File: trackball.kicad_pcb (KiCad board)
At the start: 2 copper layers, 27.5 x 35.2 mm, 38 parts, among them P1 CONN_10, P2 CONN_5, U1 MKL03Z32VFK4, U2 ADNS-3530, U4 ESD

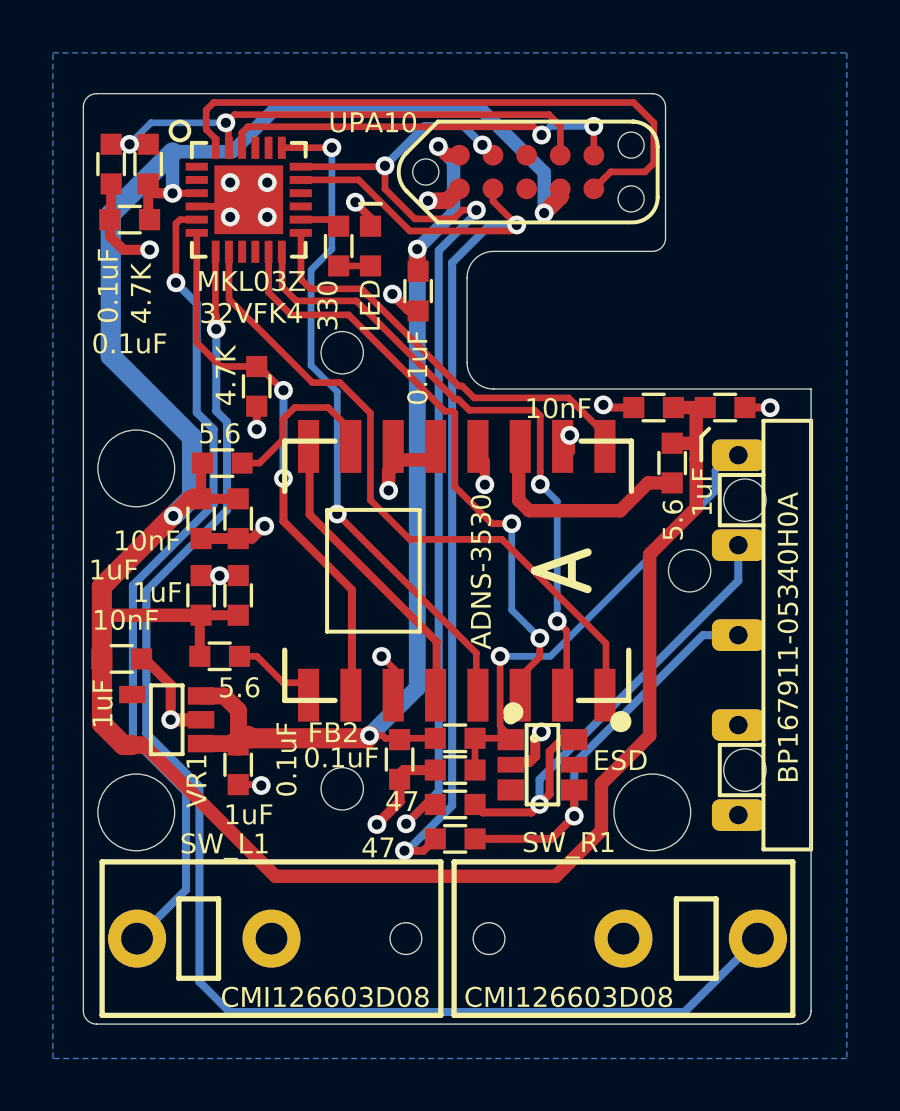
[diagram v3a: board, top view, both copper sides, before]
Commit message: Add additional silk screen content for the sensor.
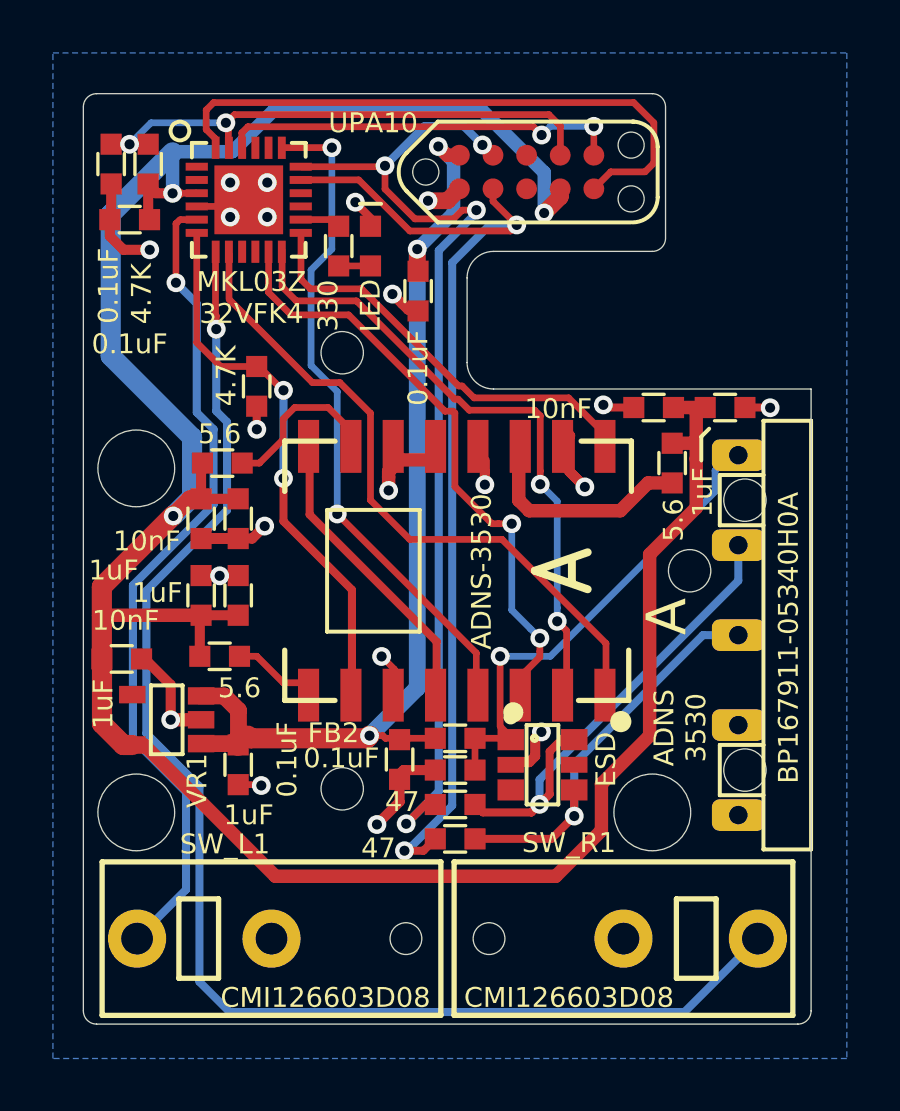
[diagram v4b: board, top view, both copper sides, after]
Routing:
- net GND: track 34.3 -> 37.0 mm
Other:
- board text added: "A"
- board text added: "ADNS 3530"
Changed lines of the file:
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@@
   (general
     (thickness 1.6)
-    (drawings 45)
-    (tracks 399)
+    (drawings 47)
+    (tracks 402)
     (zones 0)
     (modules 38)
@@
       (effects (font (size 0.75 0.75) (thickness 0.15)))
     )
-    (fp_text value ESD (at -0.15 -2.95 180) (layer F.SilkS)
+    (fp_text value ESD (at -0.2 -2.4 270) (layer F.SilkS)
       (effects (font (size 0.75 0.75) (thickness 0.15)))
     )
@@
     (pad 1 thru_hole roundrect (at -2.75 -6.8) (size 2 1.2) (drill 0.7) (layers *.Cu *.Mask) (roundrect_rratio 0.25)
       (net 4 /VCC_BOTTOM) (clearance 0.0762))
+  )
+  (gr_text "ADNS\n3530" (at 204.7 136.5 90) (layer F.SilkS)
+    (effects (font (size 0.75 0.75) (thickness 0.15)))
+  )
+  (gr_text A (at 204.2 132.3 90) (layer F.SilkS)
+    (effects (font (size 1.5 1.5) (thickness 0.3)) (justify mirror))
   )
   (gr_circle (center 198.397133 135.916091) (end 198.577411 135.916091) (layer F.SilkS) (width 0.4))
@@
   (segment (start 186.6 130.75) (end 187.2904 130.75) (width 0.381) (layer F.Cu) (net 1))
   (segment (start 187.2904 130.75) (end 187.2996 130.7592) (width 0.381) (layer F.Cu) (net 1))
-  (segment (start 200.533 125.4506) (end 200.550001 125.467601) (width 0.381) (layer F.Cu) (net 1))
-  (via (at 200.533 125.4506) (size 0.7112) (drill 0.381) (layers F.Cu B.Cu) (net 1))
   (segment (start 197.358 127.4826) (end 197.350001 127.474601) (width 0.381) (layer F.Cu) (net 1))
   (via (at 193.421 133.8072) (size 0.7112) (drill 0.381) (layers F.Cu B.Cu) (net 1))
@@
   (segment (start 188.8404 138.65) (end 188.8744 138.684) (width 0.254) (layer F.Cu) (net 1))
   (segment (start 195.4 126.379003) (end 194.150001 126.379003) (width 0.508) (layer F.Cu) (net 1))
-  (segment (start 200.533 126.067) (end 200.533 125.4506) (width 0.381) (layer F.Cu) (net 1))
-  (segment (start 200.3 126.3) (end 200.533 126.067) (width 0.381) (layer F.Cu) (net 1))
   (segment (start 193.421 133.8072) (end 193.9 134.2862) (width 0.254) (layer F.Cu) (net 1))
   (segment (start 193.9 134.2862) (end 193.9 134.6) (width 0.254) (layer F.Cu) (net 1))
@@
   (segment (start 198.3 137.8) (end 199 137.8) (width 0.381) (layer F.Cu) (net 1))
   (segment (start 199 137.8) (end 199.22489 137.57511) (width 0.381) (layer F.Cu) (net 1))
+  (segment (start 200.533 125.4506) (end 200.533 126.833) (width 0.381) (layer F.Cu) (net 1))
+  (segment (start 200.3 126.6) (end 200.744401 127.044401) (width 0.381) (layer F.Cu) (net 1))
+  (segment (start 200.533 126.833) (end 201.1 127.4) (width 0.381) (layer F.Cu) (net 1))
+  (via (at 201.1 127.4) (size 0.7112) (drill 0.381) (layers F.Cu B.Cu) (net 1))
+  (segment (start 200.744401 127.044401) (end 201.1 127.4) (width 0.381) (layer F.Cu) (net 1))
+  (segment (start 200.550001 125.467601) (end 200.533 125.4506) (width 0.381) (layer F.Cu) (net 1))
+  (segment (start 200.3 126.3) (end 200.3 126.6) (width 0.381) (layer F.Cu) (net 1))
   (segment (start 200.7 138.75) (end 200.7 139.8378) (width 0.3048) (layer F.Cu) (net 2))
   (segment (start 199.8378 140.7) (end 196.95 140.7) (width 0.3048) (layer F.Cu) (net 2))

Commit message: Disconnect pin 5 of the pogo pin connector.
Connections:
- P2 pad 5: GND -> Net-(P2-Pad5)
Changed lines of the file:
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@@
     (zones 0)
     (modules 38)
-    (nets 37)
+    (nets 38)
   )
   (page A3)
@@
   (net 35 "Net-(U1-Pad1)")
   (net 36 "Net-(U1-Pad15)")
+  (net 37 "Net-(P2-Pad5)")
   (net_class Default "This is the default net class."
     (clearance 0.2032)
@@
     (add_net "Net-(P1-Pad5)")
     (add_net "Net-(P1-Pad6)")
+    (add_net "Net-(P2-Pad5)")
     (add_net "Net-(R3-Pad1)")
     (add_net "Net-(R5-Pad1)")
@@
       (clearance 0.00254))
     (pad 5 thru_hole roundrect (at -2.75 6.8) (size 2 1.2) (drill 0.7) (layers *.Cu *.Mask) (roundrect_rratio 0.25)
-      (net 1 GND) (clearance 0.0762))
+      (net 37 "Net-(P2-Pad5)") (clearance 0.0762))
     (pad 4 thru_hole roundrect (at -2.75 3.4) (size 2 1.2) (drill 0.7) (layers *.Cu *.Mask) (roundrect_rratio 0.25)
       (net 1 GND) (clearance 0.0762))

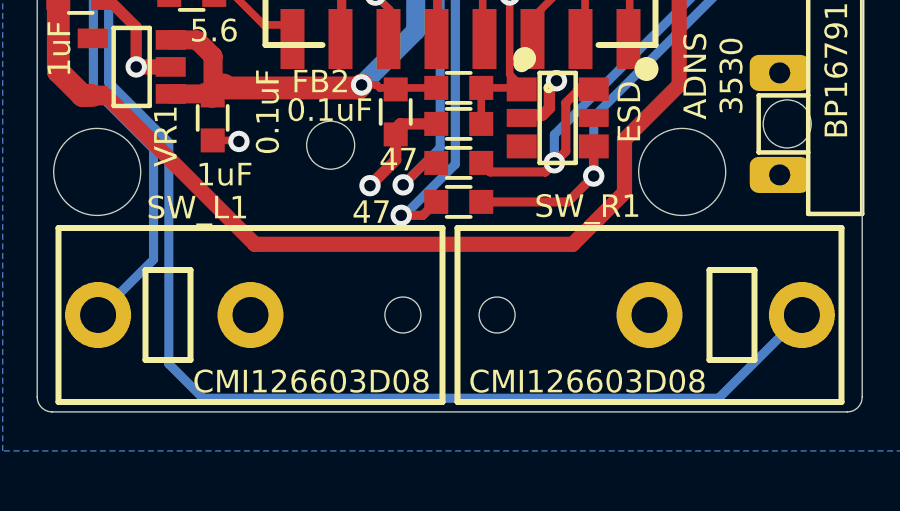
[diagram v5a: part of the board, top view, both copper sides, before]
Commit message: Update Kailh microswitches.
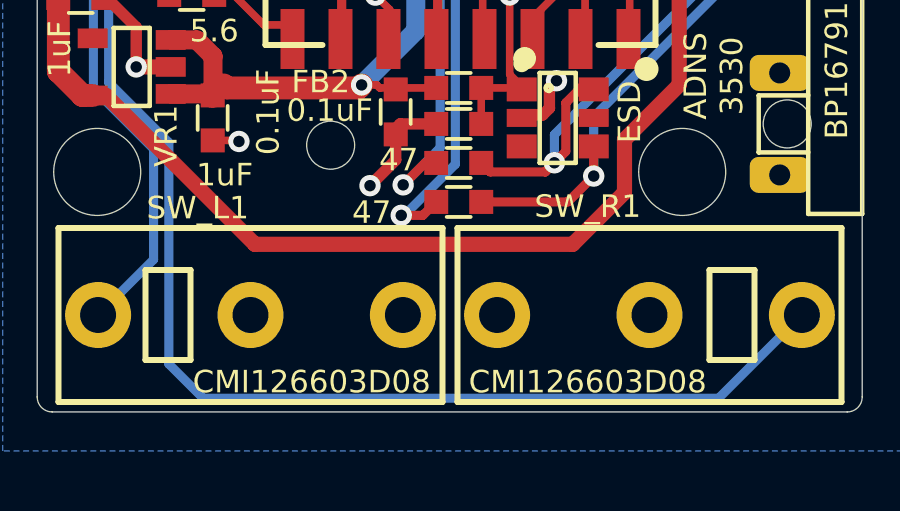
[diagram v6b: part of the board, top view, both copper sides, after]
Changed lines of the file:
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@@
     (add_net "Net-(VR1-Pad4)")
+  )
+  (module ugl:CMI126603D08 locked (layer F.Cu)
+    (at 202.560004 144.468997 180)
+    (fp_text reference SW_R1 (at 2.060004 3.618997) (layer F.SilkS)
+      (effects (font (size 0.75 0.75) (thickness 0.15)))
+    )
+    (fp_text value CMI126603D08 (at 2.060004 -2.231003) (layer F.SilkS)
+      (effects (font (size 0.75 0.75) (thickness 0.15)))
+    )
+    (fp_line (start -3.5 1.5) (end -3.5 -1.5) (layer F.SilkS) (width 0.2))
+    (fp_line (start -2 1.5) (end -3.5 1.5) (layer F.SilkS) (width 0.2))
+    (fp_line (start -2 -1.5) (end -2 1.5) (layer F.SilkS) (width 0.2))
+    (fp_line (start -3.5 -1.5) (end -2 -1.5) (layer F.SilkS) (width 0.2))
+    (fp_line (start 6.4 -2.9) (end 6.4 2.9) (layer F.SilkS) (width 0.2))
+    (fp_line (start -6.4 2.9) (end 6.4 2.9) (layer F.SilkS) (width 0.2))
+    (fp_line (start -6.4 -2.9) (end -6.4 2.9) (layer F.SilkS) (width 0.2))
+    (fp_line (start 6.4 -2.9) (end -6.4 -2.9) (layer F.SilkS) (width 0.2))
+    (pad "" thru_hole circle (at 5.08 0 180) (size 2.2 2.2) (drill 1.2) (layers *.Cu *.Mask))
+    (pad 2 thru_hole circle (at 0 0 180) (size 2.2 2.2) (drill 1.2) (layers *.Cu *.Mask)
+      (net 1 GND))
+    (pad 1 thru_hole circle (at -5.08 0 180) (size 2.2 2.2) (drill 1.2) (layers *.Cu *.Mask)
+      (net 6 /KEY_MRIGHT))
+  )
+  (module ugl:CMI126603D08 locked (layer F.Cu)
+    (at 189.260001 144.468997)
+    (fp_text reference SW_L1 (at -1.760001 -3.568997) (layer F.SilkS)
+      (effects (font (size 0.75 0.75) (thickness 0.15)))
+    )
+    (fp_text value CMI126603D08 (at 2.039999 2.231003) (layer F.SilkS)
+      (effects (font (size 0.75 0.75) (thickness 0.15)))
+    )
+    (fp_line (start -3.5 1.5) (end -3.5 -1.5) (layer F.SilkS) (width 0.2))
+    (fp_line (start -2 1.5) (end -3.5 1.5) (layer F.SilkS) (width 0.2))
+    (fp_line (start -2 -1.5) (end -2 1.5) (layer F.SilkS) (width 0.2))
+    (fp_line (start -3.5 -1.5) (end -2 -1.5) (layer F.SilkS) (width 0.2))
+    (fp_line (start 6.4 -2.9) (end 6.4 2.9) (layer F.SilkS) (width 0.2))
+    (fp_line (start -6.4 2.9) (end 6.4 2.9) (layer F.SilkS) (width 0.2))
+    (fp_line (start -6.4 -2.9) (end -6.4 2.9) (layer F.SilkS) (width 0.2))
+    (fp_line (start 6.4 -2.9) (end -6.4 -2.9) (layer F.SilkS) (width 0.2))
+    (pad "" thru_hole circle (at 5.08 0) (size 2.2 2.2) (drill 1.2) (layers *.Cu *.Mask))
+    (pad 2 thru_hole circle (at 0 0) (size 2.2 2.2) (drill 1.2) (layers *.Cu *.Mask)
+      (net 1 GND))
+    (pad 1 thru_hole circle (at -5.08 0) (size 2.2 2.2) (drill 1.2) (layers *.Cu *.Mask)
+      (net 5 /KEY_MLEFT))
   )
   (module ugl:ADNS-3530 locked (layer F.Cu)
@@
     )
   )
-  (module ugl:CMI126603D08 locked (layer F.Cu)
-    (at 202.560004 144.468997 180)
-    (fp_text reference SW_R1 (at 2.060004 3.618997) (layer F.SilkS)
-      (effects (font (size 0.75 0.75) (thickness 0.15)))
-    )
-    (fp_text value CMI126603D08 (at 2.060004 -2.231003) (layer F.SilkS)
-      (effects (font (size 0.75 0.75) (thickness 0.15)))
-    )
-    (fp_line (start -3.5 1.5) (end -3.5 -1.5) (layer F.SilkS) (width 0.2))
-    (fp_line (start -2 1.5) (end -3.5 1.5) (layer F.SilkS) (width 0.2))
-    (fp_line (start -2 -1.5) (end -2 1.5) (layer F.SilkS) (width 0.2))
-    (fp_line (start -3.5 -1.5) (end -2 -1.5) (layer F.SilkS) (width 0.2))
-    (fp_line (start 6.4 -2.9) (end 6.4 2.9) (layer F.SilkS) (width 0.2))
-    (fp_line (start -6.4 2.9) (end 6.4 2.9) (layer F.SilkS) (width 0.2))
-    (fp_line (start -6.4 -2.9) (end -6.4 2.9) (layer F.SilkS) (width 0.2))
-    (fp_line (start 6.4 -2.9) (end -6.4 -2.9) (layer F.SilkS) (width 0.2))
-    (pad "" np_thru_hole circle (at 5.08 0 180) (size 1.2 1.2) (drill 1.2) (layers *.Cu *.Mask))
-    (pad 2 thru_hole circle (at 0 0 180) (size 2.2 2.2) (drill 1.2) (layers *.Cu *.Mask)
-      (net 1 GND))
-    (pad 1 thru_hole circle (at -5.08 0 180) (size 2.2 2.2) (drill 1.2) (layers *.Cu *.Mask)
-      (net 6 /KEY_MRIGHT))
-  )
-  (module ugl:CMI126603D08 locked (layer F.Cu)
-    (at 189.260001 144.468997)
-    (fp_text reference SW_L1 (at -1.760001 -3.568997) (layer F.SilkS)
-      (effects (font (size 0.75 0.75) (thickness 0.15)))
-    )
-    (fp_text value CMI126603D08 (at 2.039999 2.231003) (layer F.SilkS)
-      (effects (font (size 0.75 0.75) (thickness 0.15)))
-    )
-    (fp_line (start -3.5 1.5) (end -3.5 -1.5) (layer F.SilkS) (width 0.2))
-    (fp_line (start -2 1.5) (end -3.5 1.5) (layer F.SilkS) (width 0.2))
-    (fp_line (start -2 -1.5) (end -2 1.5) (layer F.SilkS) (width 0.2))
-    (fp_line (start -3.5 -1.5) (end -2 -1.5) (layer F.SilkS) (width 0.2))
-    (fp_line (start 6.4 -2.9) (end 6.4 2.9) (layer F.SilkS) (width 0.2))
-    (fp_line (start -6.4 2.9) (end 6.4 2.9) (layer F.SilkS) (width 0.2))
-    (fp_line (start -6.4 -2.9) (end -6.4 2.9) (layer F.SilkS) (width 0.2))
-    (fp_line (start 6.4 -2.9) (end -6.4 -2.9) (layer F.SilkS) (width 0.2))
-    (pad "" np_thru_hole circle (at 5.08 0) (size 1.2 1.2) (drill 1.2) (layers *.Cu *.Mask))
-    (pad 2 thru_hole circle (at 0 0) (size 2.2 2.2) (drill 1.2) (layers *.Cu *.Mask)
-      (net 1 GND))
-    (pad 1 thru_hole circle (at -5.08 0) (size 2.2 2.2) (drill 1.2) (layers *.Cu *.Mask)
-      (net 5 /KEY_MLEFT))
-  )
   (module ugl:hole_2.9mm locked (layer F.Cu)

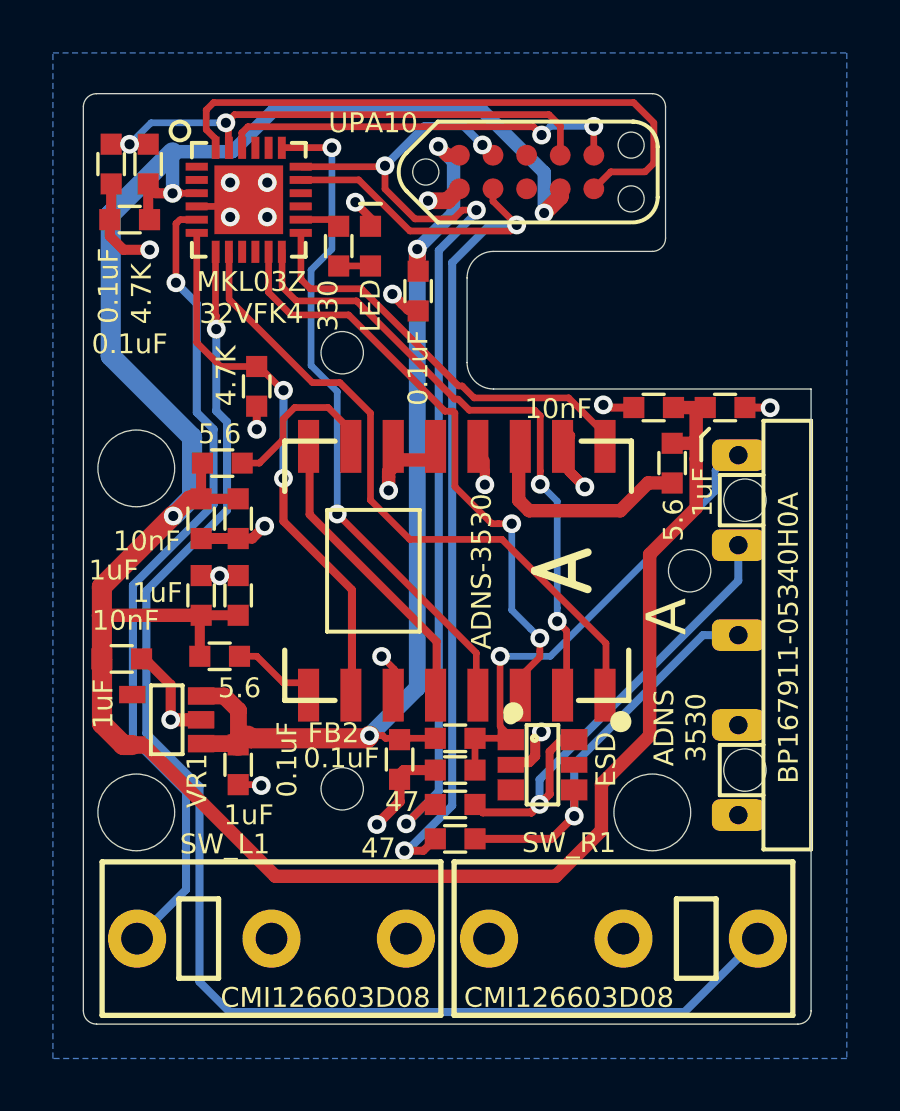
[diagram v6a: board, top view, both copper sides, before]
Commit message: Replace resistors from 4.7K to 5.1K and from 47 to 33 ohms.
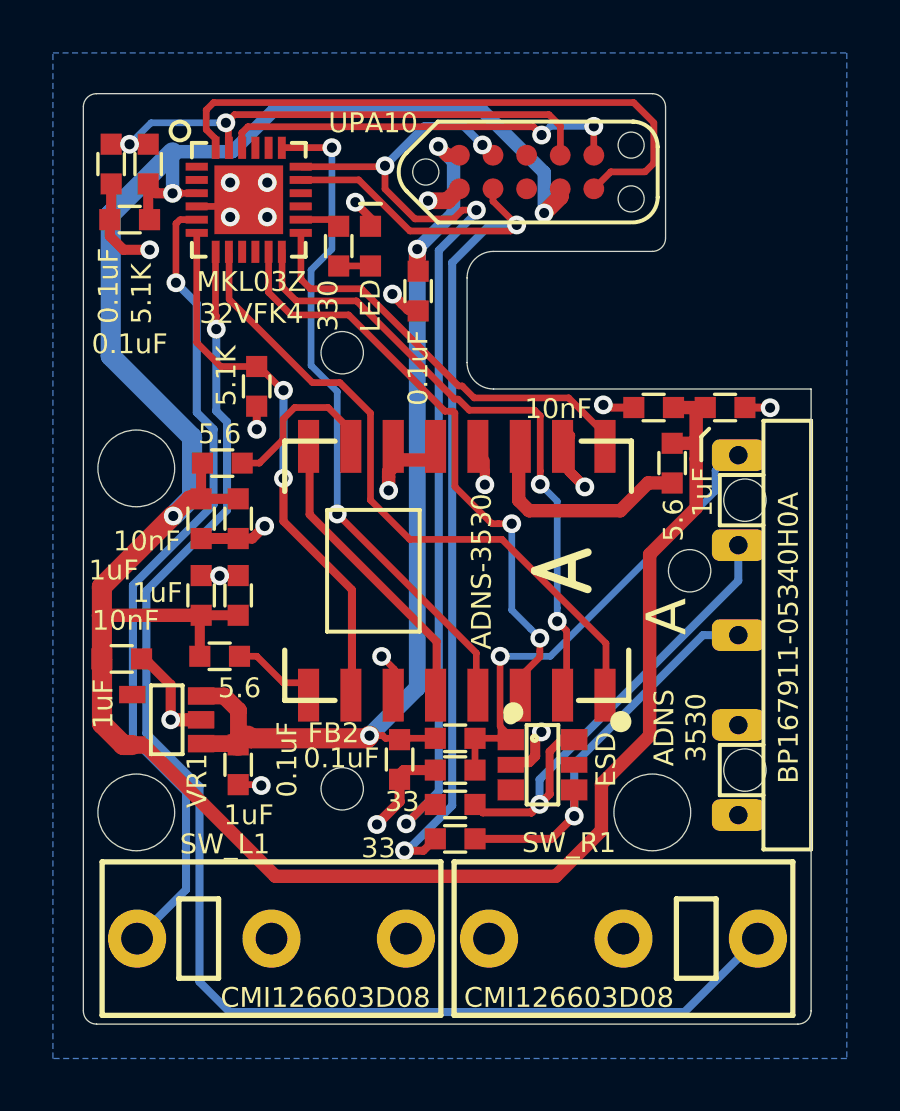
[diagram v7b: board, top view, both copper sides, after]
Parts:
- R1, R4: value 4.7K -> 5.1K
- R6, R7: value 47 -> 33
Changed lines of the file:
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@@
-(kicad_pcb (version 20171130) (host pcbnew 5.1.5-52549c5~84~ubuntu18.04.1)
+(kicad_pcb (version 20171130) (host pcbnew 5.1.5-52549c5~86~ubuntu18.04.1)
   (general
     (thickness 1.6)
@@
       (effects (font (size 0.75 0.75) (thickness 0.15)))
     )
-    (fp_text value 47 (at -2 -0.1) (layer F.SilkS)
+    (fp_text value 33 (at -2 -0.1) (layer F.SilkS)
       (effects (font (size 0.75 0.75) (thickness 0.15)))
     )
@@
       (effects (font (size 0.75 0.75) (thickness 0.15)))
     )
-    (fp_text value 4.7K (at -4.9 -0.25 270) (layer F.SilkS)
+    (fp_text value 5.1K (at -4.9 -0.25 270) (layer F.SilkS)
       (effects (font (size 0.75 0.75) (thickness 0.15)))
     )
@@
       (effects (font (size 0.75 0.75) (thickness 0.15)))
     )
-    (fp_text value 4.7K (at -0.4 1.15 90) (layer F.SilkS)
+    (fp_text value 5.1K (at -0.4 1.15 90) (layer F.SilkS)
       (effects (font (size 0.75 0.75) (thickness 0.15)))
     )
@@
       (effects (font (size 0.75 0.75) (thickness 0.15)))
     )
-    (fp_text value 47 (at -2.9 0.35 180) (layer F.SilkS)
-      (effects (font (size 0.75 0.75) (thickness 0.15)))
-    )
+    (fp_text value 33 (at -2.9 0.35 180) (layer F.SilkS)
+      (effects (font (size 0.75 0.75) (thickness 0.15)))
+    )
